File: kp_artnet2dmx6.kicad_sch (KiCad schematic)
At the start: 98 parts, among them IC1 KSZ8081MNXIA-TR, IC2 M95640-RMN6P, IC3 AP2281-3WG-7, IC4 MP2331HGTL-P, J1 RJ45_Amphenol_RJMG1BD3B8K1ANR, J10 DMX, J11 DMX, J12 DMX, J14 SWD, J15 USB-B-S-RA, J2 SCREEN, J3 BTN, J5 BTN, J7 DMX, J8 DMX, J9 DMX, Q1 AO3401A, SW1 SW_SPDT, U1 STM32F407VGT6, U2 MCP23S17_SP, U3 USBLC6-2SC6, Y1 ASDDV-25.000MHZ-LC-T

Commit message: main board : start doing sig gnd gnd sigpow
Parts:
- IC1: footprint SamacSys:QFN50P500X500X100-33N-D -> QFN50P500X500X100-33N-D
- IC2: footprint SamacSys:SOIC127P600X175-8N -> SOIC127P600X175-8N
- IC3: footprint SamacSys:SOT95P285X140-6N -> SOT95P285X140-6N
- IC4: footprint Package_TO_SOT_SMD:SOT-583-8 -> MP2331HGTLP
- J15: footprint SamacSys:USBBSRA -> USBBSRA
- Y1: footprint SamacSys:AbraconASDDV -> AbraconASDDV
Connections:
- net GND: now also J10.3 (Pin_3), J10.5 (Pin_5), J11.3 (Pin_3), J11.5 (Pin_5), J12.3 (Pin_3), J12.5 (Pin_5), J2.3 (Pin_3), J2.5 (Pin_5), J7.3 (Pin_3), J7.5 (Pin_5), J8.3 (Pin_3), J8.5 (Pin_5), J9.3 (Pin_3), J9.5 (Pin_5)
- net STM_I2C1_SCL: now also J2.6 (Pin_6); no longer J2.4 (Pin_4)
- net STM_I2C1_SDA: now also J2.4 (Pin_4); no longer J2.3 (Pin_3)
- net STM_UART4_RX: now also J10.4 (Pin_4); no longer J10.3 (Pin_3)
- net STM_UART4_TX: now also J10.6 (Pin_6); no longer J10.4 (Pin_4)
- net STM_UART5_RX: now also J11.4 (Pin_4); no longer J11.3 (Pin_3)
- net STM_UART5_TX: now also J11.6 (Pin_6); no longer J11.4 (Pin_4)
- net STM_USART1_RX: now also J7.4 (Pin_4); no longer J7.3 (Pin_3)
- net STM_USART1_TX: now also J7.6 (Pin_6); no longer J7.4 (Pin_4)
- net STM_USART2_RX: now also J8.4 (Pin_4); no longer J8.3 (Pin_3)
- net STM_USART2_TX: now also J8.6 (Pin_6); no longer J8.4 (Pin_4)
- net STM_USART3_RX: now also J9.4 (Pin_4); no longer J9.3 (Pin_3)
- net STM_USART3_TX: now also J9.6 (Pin_6); no longer J9.4 (Pin_4)
- net STM_USART6_RX: now also J12.4 (Pin_4); no longer J12.3 (Pin_3)
- net STM_USART6_TX: now also J12.6 (Pin_6); no longer J12.4 (Pin_4)
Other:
- moved on the sheet: J2, R24, R25

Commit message: DRC OK
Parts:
- L1: footprint Inductor_SMD:L_0805_2012Metric -> homemade_footprints:L_Bourns_SRP4020CC
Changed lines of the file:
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@@
 			)
 		)
-		(property "Footprint" "Inductor_SMD:L_0805_2012Metric"
+		(property "Footprint" "homemade_footprints:L_Bourns_SRP4020CC"
 			(at 172.72 275.59 0)
 			(hide yes)

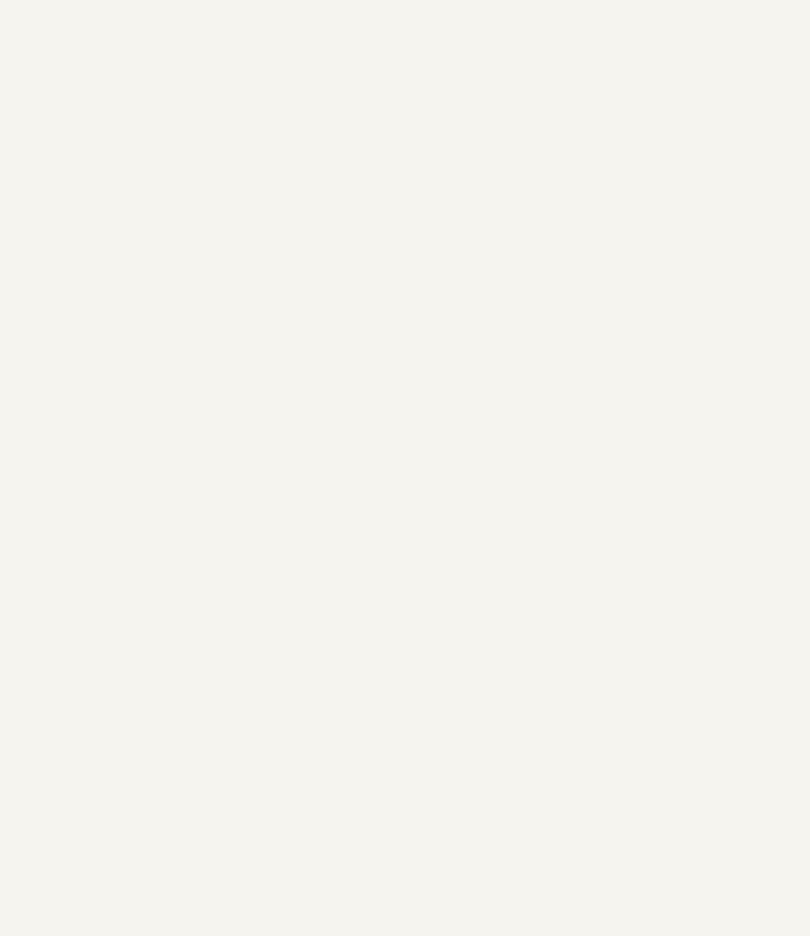
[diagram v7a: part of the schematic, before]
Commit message: add pwr leds
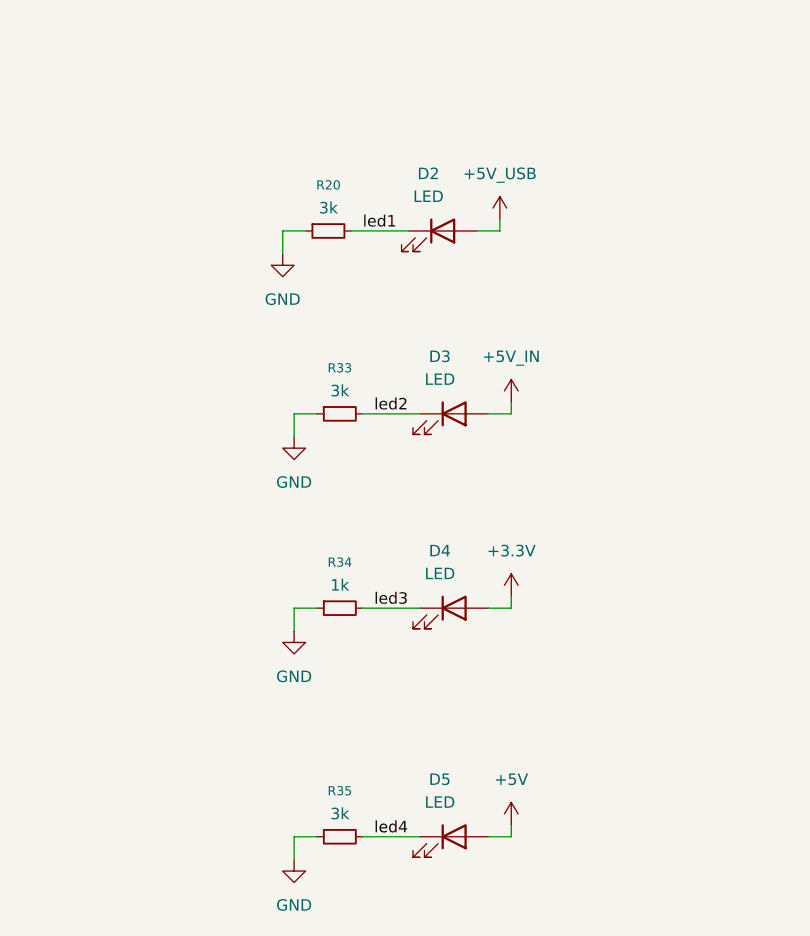
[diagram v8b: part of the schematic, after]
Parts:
- added D2, D3, D4, D5: LED, LED_SMD:LED_0805_2012Metric, symbol Device:LED
- added R20, R33, R35: 3k, Resistor_SMD:R_0805_2012Metric, symbol Device:R_Small
- added R34: 1k, Resistor_SMD:R_0603_1608Metric, symbol Device:R_Small
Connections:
- net +3.3V: now also D4.2 (A)
- net +5V: now also D5.2 (A)
- net +5V_IN: now also D3.2 (A)
- net +5V_USB: now also D2.2 (A)
- net GND: now also R20.1, R33.1, R34.1, R35.1
- new net led1: D2.1 (K), R20.2
- new net led2: D3.1 (K), R33.2
- new net led3: D4.1 (K), R34.2
- new net led4: D5.1 (K), R35.2
